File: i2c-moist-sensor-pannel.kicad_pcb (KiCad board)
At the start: 2 copper layers, 100 x 150 mm, 140 parts, among them IC1 ATTINY441-SSU, P1 CONN_02X03, X1 16MHz

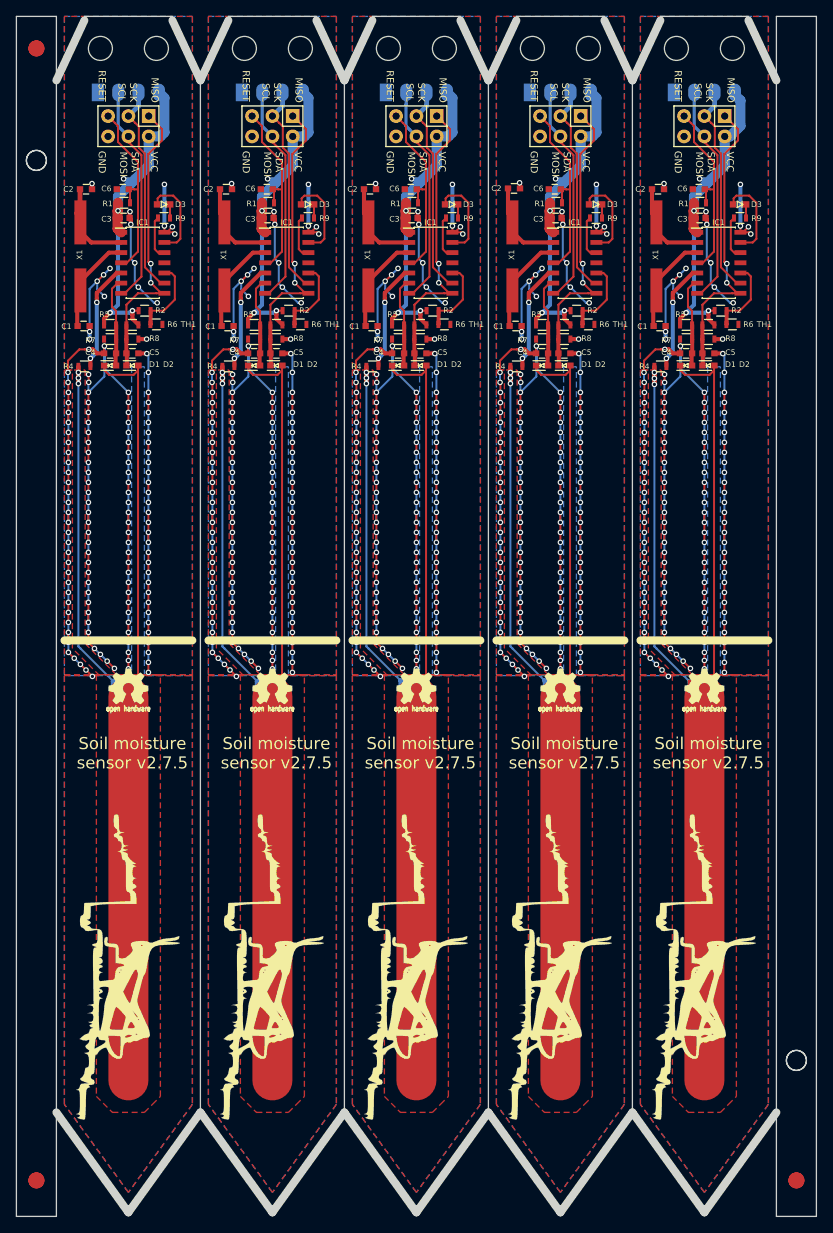
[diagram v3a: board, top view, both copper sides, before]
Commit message: Power thermistor and moisture sensing circuitry from a pin rather than directly so lower the power consumption
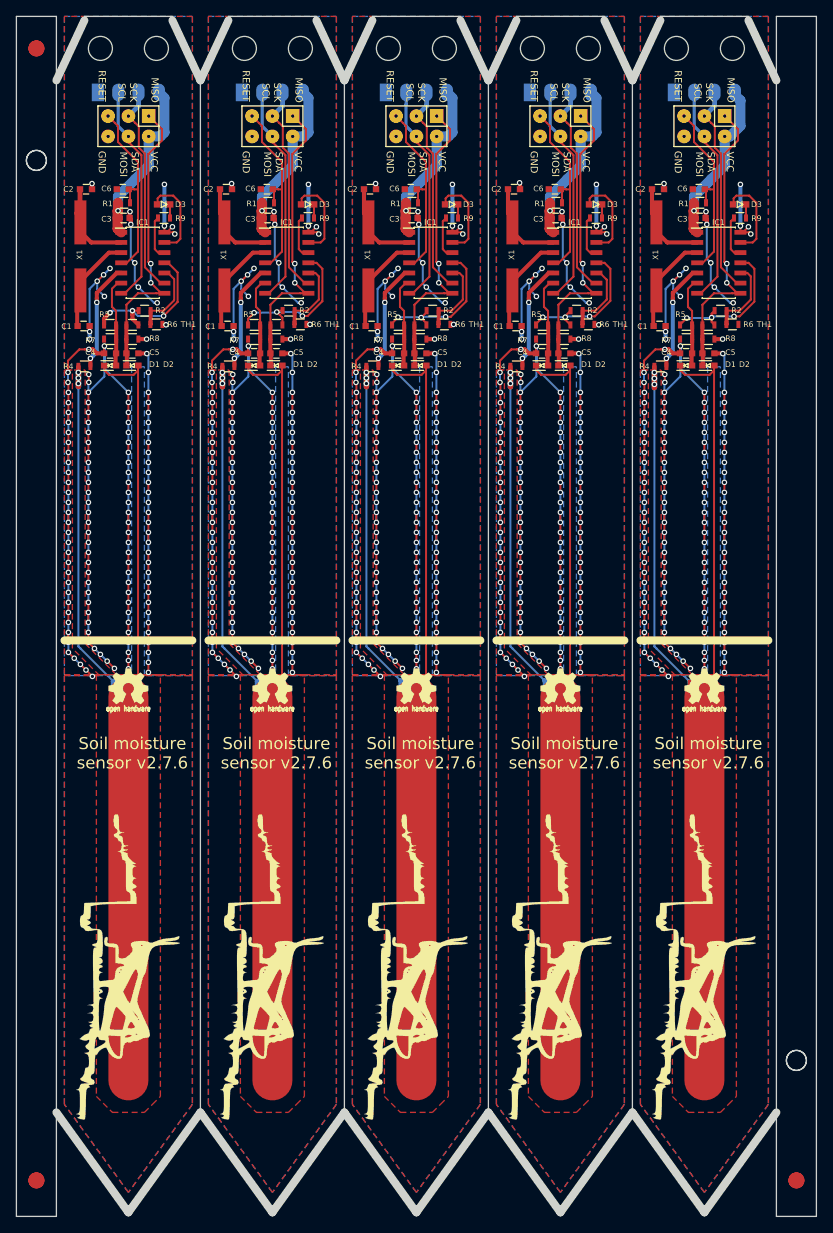
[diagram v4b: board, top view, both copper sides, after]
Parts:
- removed the REF** at (177.5, 167.5) (x2)
- removed the REF** at (82.5, 40.0) (x2)
- removed the REF** at (82.5, 167.5) (x2)
- removed the REF** at (82.5, 26.0) (x2)
- removed the REF** at (177.5, 152.5) (x2)
- added REF** (x2): Fiducial_Modern_CopperTop, Fiducials:Fiducial_Modern_CopperTop, F.Cu at (177.5, 167.5)
- added REF** (x2): MountingHole_2-5mm, Mounting_Holes:MountingHole_2-5mm, F.Cu at (82.5, 40.0)
- added REF** (x2): Fiducial_Modern_CopperTop, Fiducials:Fiducial_Modern_CopperTop, F.Cu at (82.5, 167.5)
- added REF** (x2): Fiducial_Modern_CopperTop, Fiducials:Fiducial_Modern_CopperTop, F.Cu at (82.5, 26.0)
- added REF** (x2): MountingHole_2-5mm, Mounting_Holes:MountingHole_2-5mm, F.Cu at (177.5, 152.5)
- C1: value 18p -> 33p
- C2: value 18p -> 33pp
- moved C2 0.10 mm to (142.2, 43.6)
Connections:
- IC1 pad 11: Net-(IC1-Pad11) -> /POWER (x5)
- R2 pad 1: VCC -> /POWER (x5)
- R5 pad 2: VCC -> /POWER (x5)
- R6 pad 2: VCC -> /POWER (x5)
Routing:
- net VCC: track 222.9 -> 111.8 mm, vias 20 -> 5
- net /POWER: track 0.00 -> 97.4 mm, vias 0 -> 15
- net /SENSOR_TRACK: track 750.1 -> 765.0 mm
- net GND: track 1118.4 -> 1120.3 mm, vias 720 -> 724
- net /THERMISTOR: track 48.5 -> 47.9 mm
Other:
- net class Default: clearance 0.1778 -> 0
- rule trace_clearance: 0.1778 -> 0
- board text added: "Soil moisture sensor v2.7.6"
- board text removed: "Soil moisture sensor v2.7.5"

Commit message: Shuffle stuff around
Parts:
- removed the P1 at (94.0, 35.7)
- removed the P1 at (112.0, 35.7)
- removed the P1 at (130.0, 35.7)
- removed the P1 at (148.0, 35.7)
- removed the P1 at (166.0, 35.7)
- removed the REF** at (177.5, 167.5) (x2)
- removed the REF** at (82.5, 40.0) (x2)
- removed the REF** at (82.5, 167.5) (x2)
- removed the REF** at (82.5, 26.0) (x2)
- removed the REF** at (177.5, 152.5) (x2)
- added P1: CONN_02X03, Pin_Headers:Pin_Header_Straight_2x03, F.Cu at (148.0, 37.2)
- added P1: CONN_02X03, Pin_Headers:Pin_Header_Straight_2x03, F.Cu at (130.0, 37.2)
- added P1: CONN_02X03, Pin_Headers:Pin_Header_Straight_2x03, F.Cu at (94.0, 37.2)
- added P1: CONN_02X03, Pin_Headers:Pin_Header_Straight_2x03, F.Cu at (112.0, 37.2)
- added P1: CONN_02X03, Pin_Headers:Pin_Header_Straight_2x03, F.Cu at (166.0, 37.2)
- added REF** (x2): Fiducial_Modern_CopperTop, Fiducials:Fiducial_Modern_CopperTop, F.Cu at (177.5, 167.5)
- added REF** (x2): MountingHole_2-5mm, Mounting_Holes:MountingHole_2-5mm, F.Cu at (82.5, 40.0)
- added REF** (x2): Fiducial_Modern_CopperTop, Fiducials:Fiducial_Modern_CopperTop, F.Cu at (82.5, 167.5)
- added REF** (x2): Fiducial_Modern_CopperTop, Fiducials:Fiducial_Modern_CopperTop, F.Cu at (82.5, 26.0)
- added REF** (x2): MountingHole_2-5mm, Mounting_Holes:MountingHole_2-5mm, F.Cu at (177.5, 152.5)
- moved PIN_SOCKET_4 0.50 mm to (94.0, 31.0)
- moved PIN_SOCKET_4 0.50 mm to (112.0, 31.0)
- moved PIN_SOCKET_4 0.50 mm to (130.0, 31.0)
- moved PIN_SOCKET_4 0.50 mm to (148.0, 31.0)
- moved PIN_SOCKET_4 0.50 mm to (166.0, 31.0)
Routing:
- net GND: track 1120.3 -> 1137.7 mm, vias 724 -> 734
- net /MISO/SENSE_HIGH: track 190.6 -> 176.7 mm
- net /RESET: track 120.4 -> 113.3 mm
- net /POWER: track 97.4 -> 93.7 mm
- net VCC: track 111.8 -> 113.6 mm
